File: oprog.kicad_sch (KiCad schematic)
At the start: 53 parts, among them Q1 BC857, Q2 BC857, Q3 BC847, Q4 BC847, U1 AMS1117-3.3, U2 PIC18F25K50

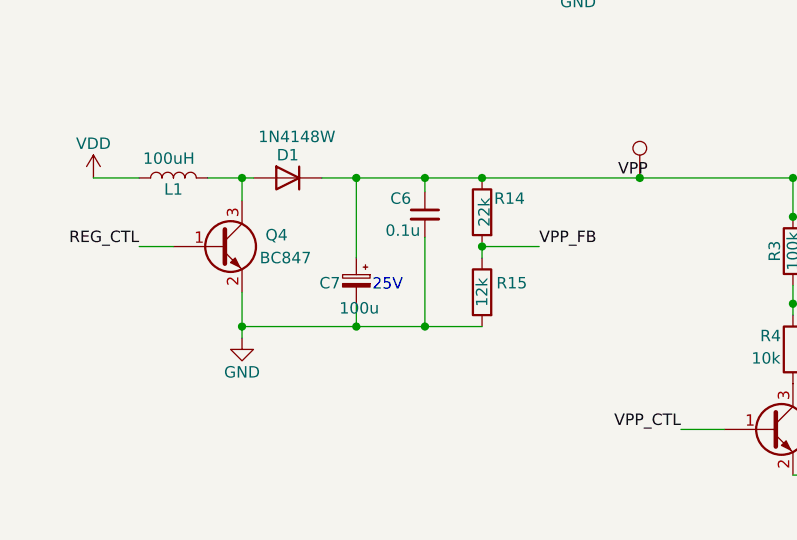
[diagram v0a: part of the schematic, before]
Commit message: Add schematic
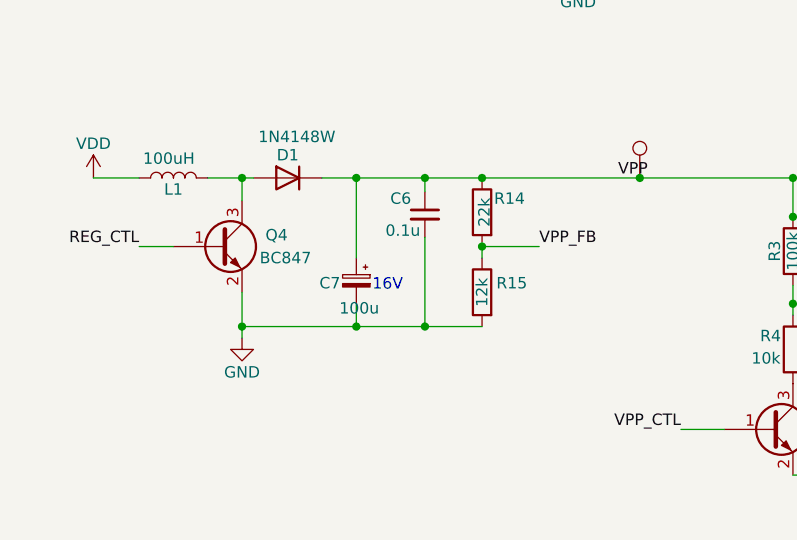
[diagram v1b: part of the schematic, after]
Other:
- note removed: "25V"
- title: Openprog+ -> Openprog All-In-One
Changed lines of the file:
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@@
   (paper "A4")
   (title_block
-    (title "Openprog+")
+    (title "Openprog All-In-One")
     (date "2023-09-02")
     (rev "1.0")
@@
     (effects (font (size 1.27 1.27)) (justify left bottom))
   )
-  (text "25V" (at 65.278 160.02 0)
+  (text "16V\n" (at 65.278 160.02 0)
     (effects (font (size 1.27 1.27)) (justify left bottom))
   )
